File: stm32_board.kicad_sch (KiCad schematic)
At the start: 13 parts, among them SW1 SW_SPDT, U1 STM32F103C8Tx

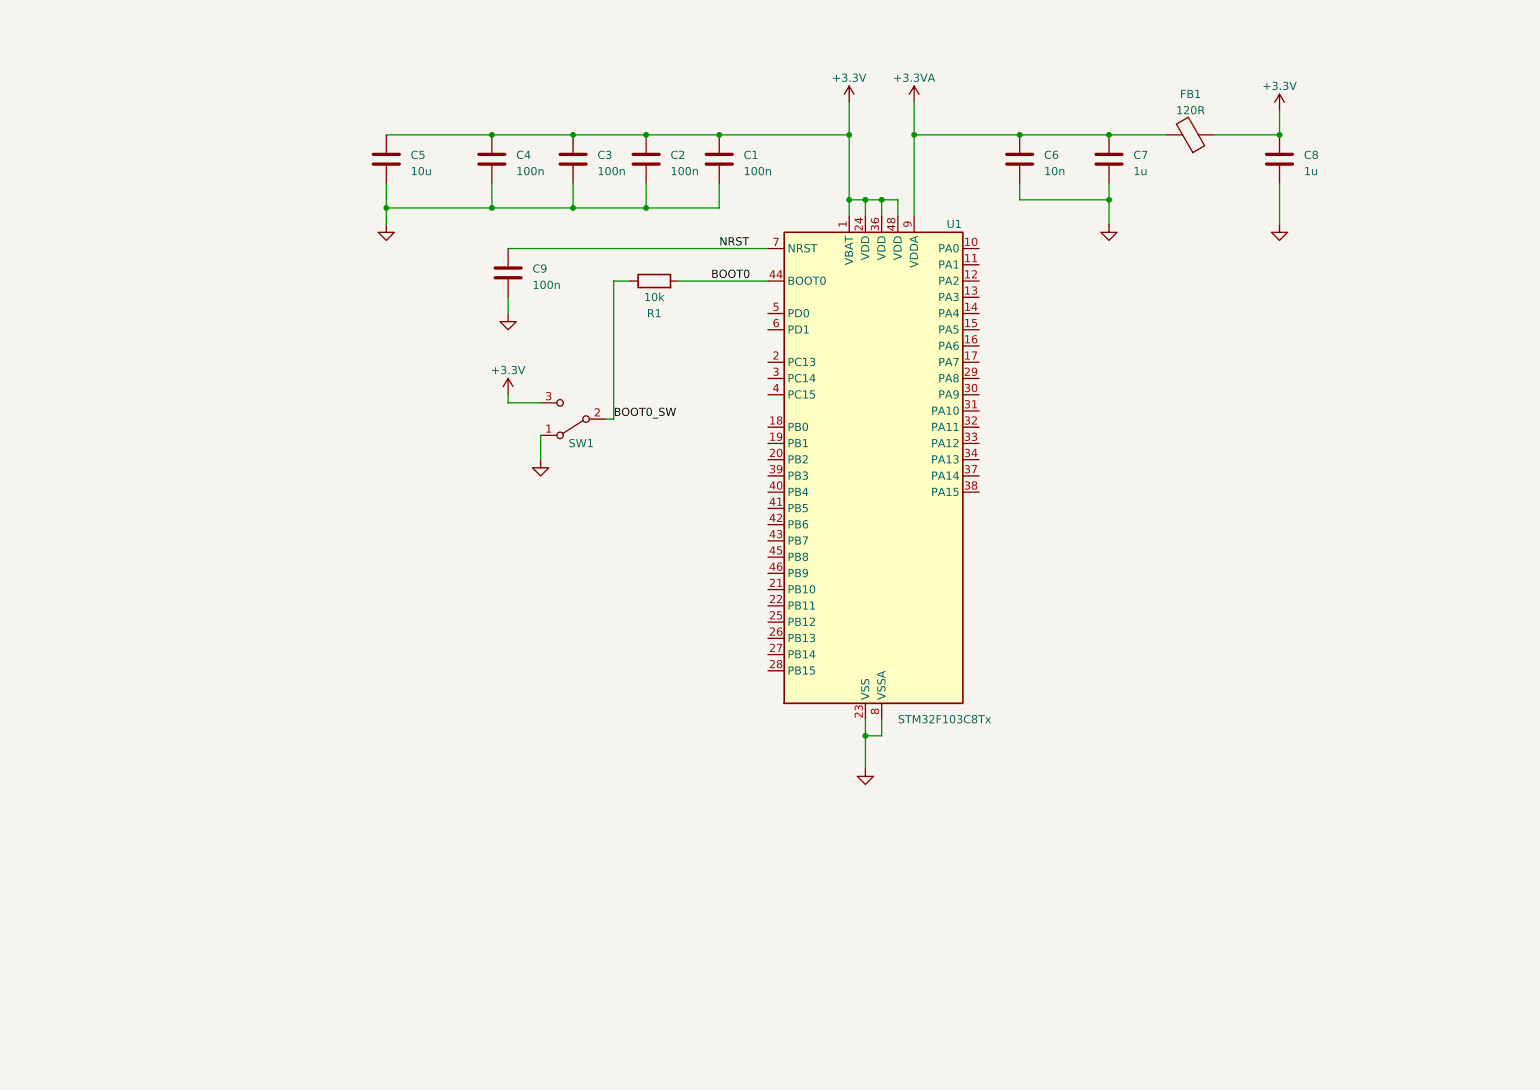
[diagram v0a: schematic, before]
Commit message: Added Crystal Oscillator
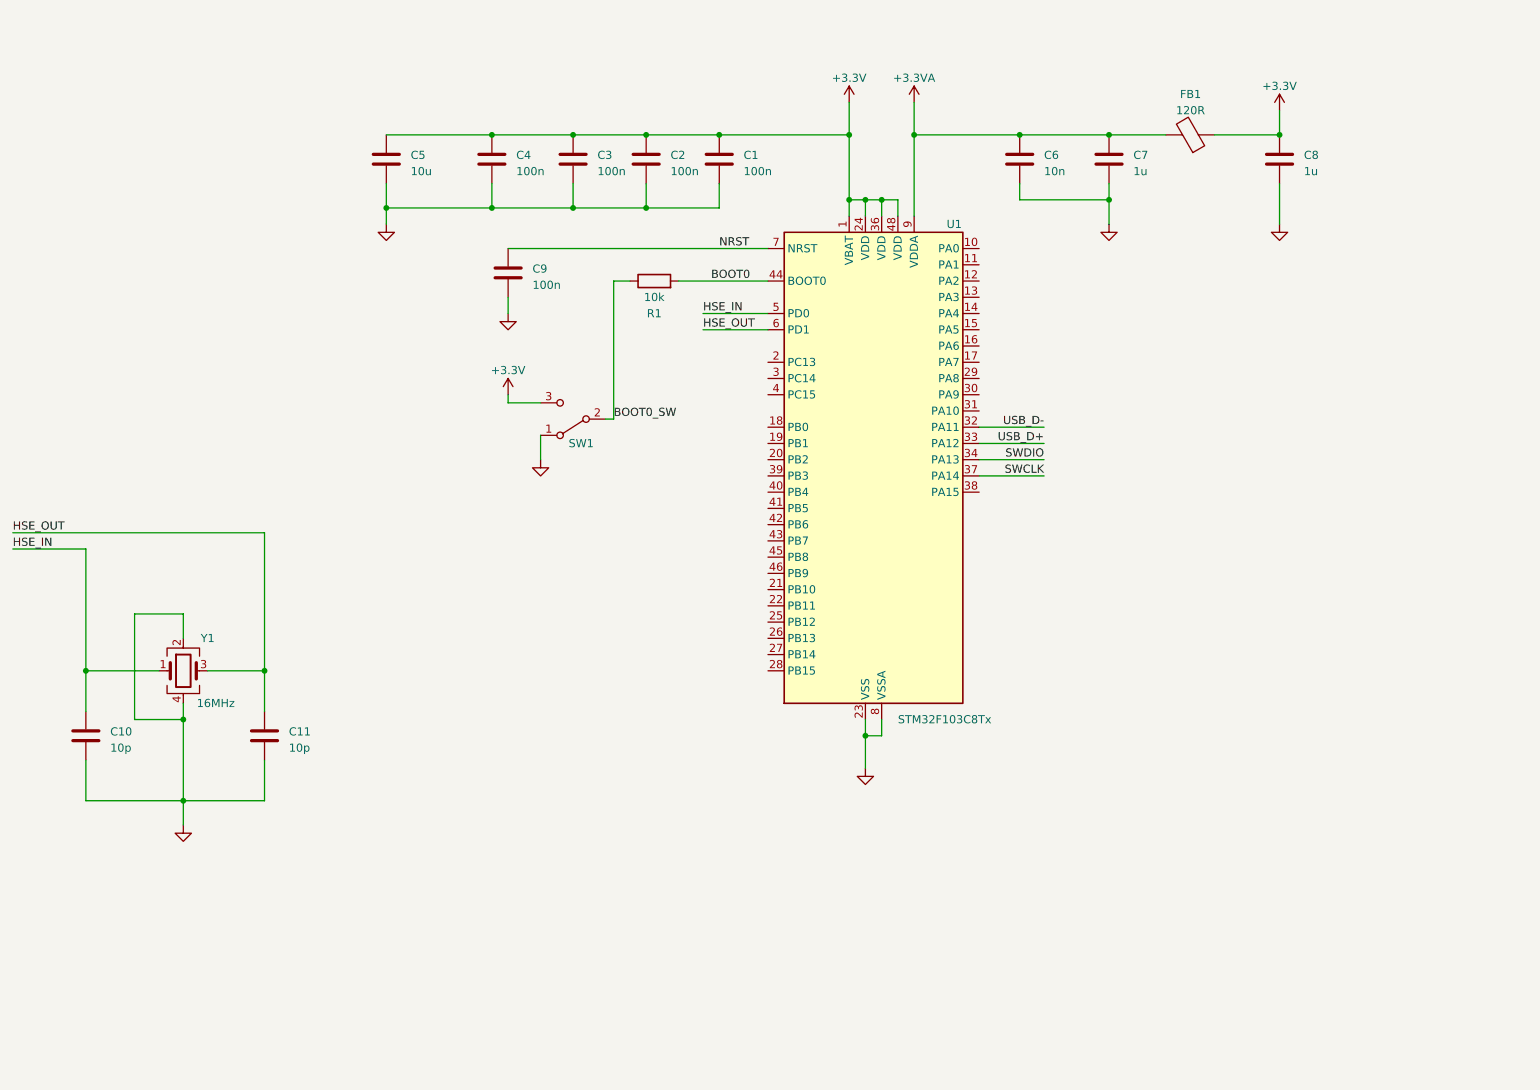
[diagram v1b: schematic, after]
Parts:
- added C10, C11: 10p, symbol Device:C
- added Y1: 16MHz, symbol Device:Crystal_GND24
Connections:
- net GND: now also C10.2, C11.2, Y1.2, Y1.4
- net USB_D-: now reaches U1.32 (PA11)
- net USB_D+: now reaches U1.33 (PA12)
- net SWDIO: now reaches U1.34 (PA13)
- net SWCLK: now reaches U1.37 (PA14)
- net HSE_IN: now reaches U1.5 (PD0)
- net HSE_IN: now also C10.1, Y1.1
- net HSE_OUT: now reaches U1.6 (PD1)
- net HSE_OUT: now also C11.1, Y1.3

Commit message: Added USB jack
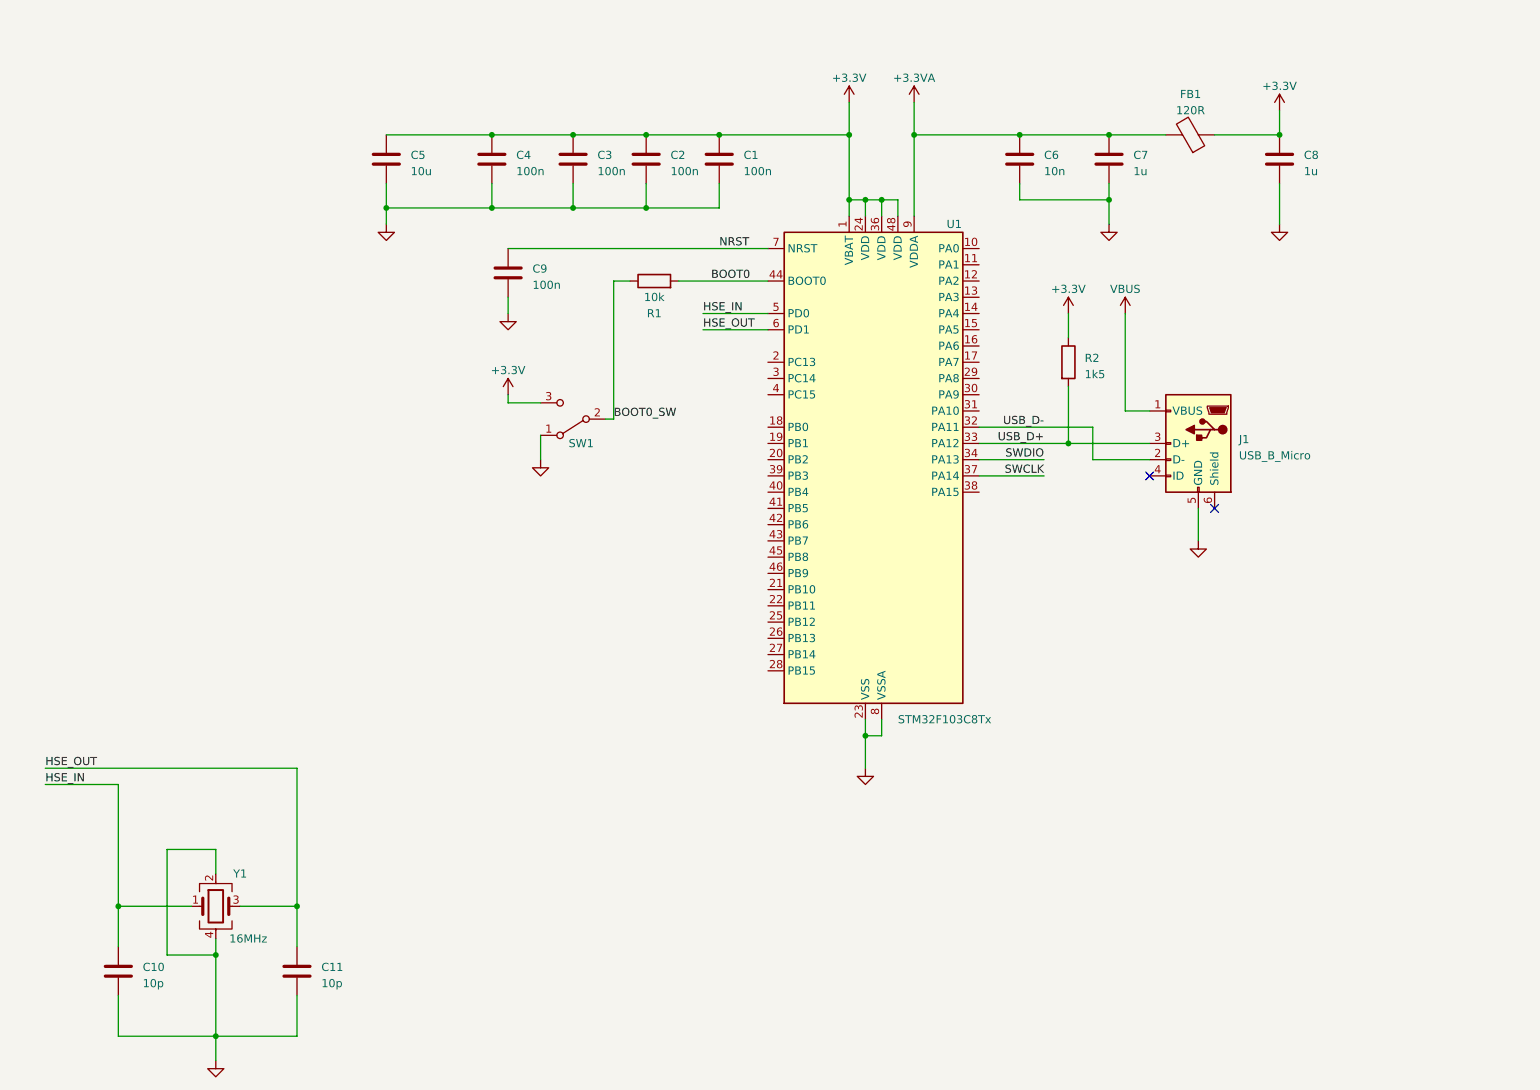
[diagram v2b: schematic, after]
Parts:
- added J1: USB_B_Micro, symbol Connector:USB_B_Micro
- added R2: 1k5, symbol Device:R
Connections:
- net +3.3V: now also R2.1
- net GND: now also J1.5 (GND)
- net USB_D+: now also J1.3 (D+), R2.2
- net USB_D-: now also J1.2 (D-)
- new net VBUS: J1.1 (VBUS)
- no-connect marks 0 -> 2
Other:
- moved on the sheet: C10, C11, Y1

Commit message: Added connectors
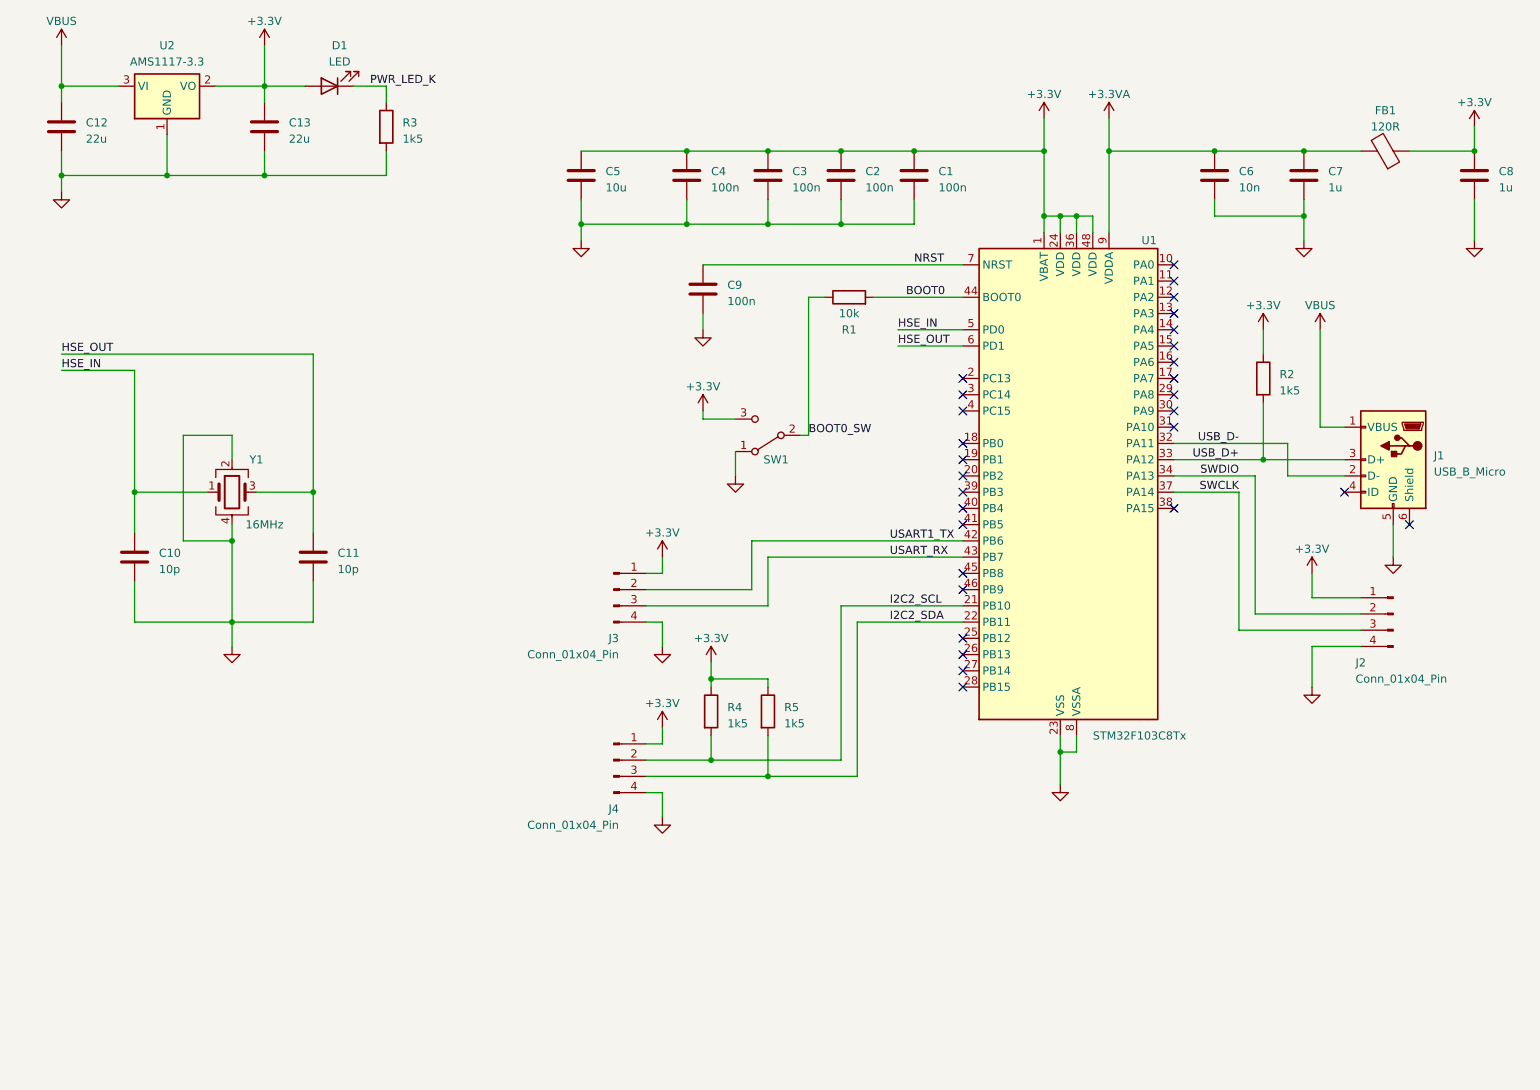
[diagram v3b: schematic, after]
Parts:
- added C12, C13: 22u, symbol Device:C
- added D1: LED, symbol Device:LED
- added J2, J3, J4: Conn_01x04_Pin, symbol Connector:Conn_01x04_Pin
- added R3, R4, R5: 1k5, symbol Device:R
- added U2: AMS1117-3.3, Package_TO_SOT_SMD:SOT-223-3_TabPin2, symbol Regulator_Linear:AMS1117-3.3
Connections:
- net +3.3V: now also C13.1, D1.2 (A), J2.1 (Pin_1), J3.1 (Pin_1), J4.1 (Pin_1), R4.1, R5.1, U2.2 (VO)
- net GND: now also C12.2, C13.2, J2.4 (Pin_4), J3.4 (Pin_4), J4.4 (Pin_4), R3.2, U2.1 (GND)
- net SWCLK: now also J2.3 (Pin_3)
- net SWDIO: now also J2.2 (Pin_2)
- net VBUS: now also C12.1, U2.3 (VI)
- net I2C2_SCL: now reaches U1.21 (PB10)
- net I2C2_SCL: now also J4.2 (Pin_2), R4.2
- net I2C2_SDA: now reaches U1.22 (PB11)
- net I2C2_SDA: now also J4.3 (Pin_3), R5.2
- net USART1_TX: now reaches U1.42 (PB6)
- net USART1_TX: now also J3.2 (Pin_2)
- net USART_RX: now reaches U1.43 (PB7)
- net USART_RX: now also J3.3 (Pin_3)
- new net PWR_LED_K: D1.1 (K), R3.1
- no-connect marks 2 -> 29
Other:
- title: (none) -> STM32 Development Board
- moved on the sheet: C1, C10, C11, C2, C3, C4, C5, C6, C7, C8, C9, FB1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

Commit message: Added notes + fixed annotations
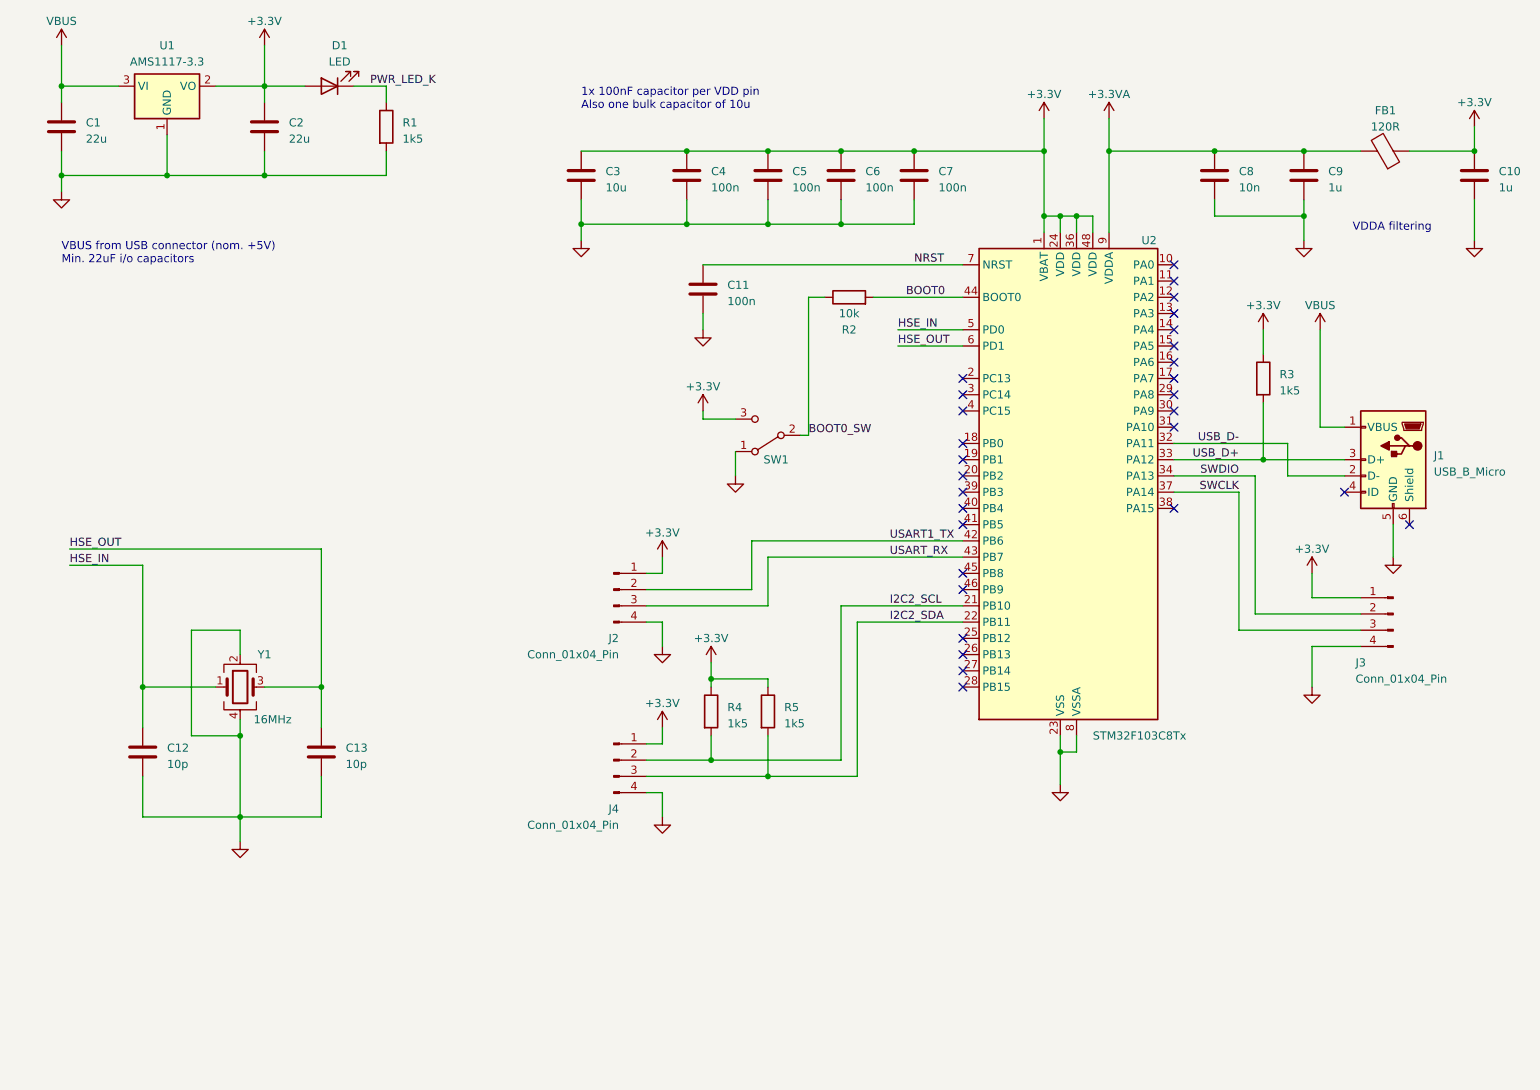
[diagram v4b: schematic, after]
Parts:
- renumbered C12 to C1, C8 to C10, C9 to C11, C10 to C12, C11 to C13, C13 to C2, C5 to C3, C3 to C5, C2 to C6, C1 to C7, C6 to C8, C7 to C9, J3 to J2, J2 to J3, R3 to R1, R1 to R2, R2 to R3, U2 to U1, U1 to U2
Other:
- note added: "1x 100nF capacitor per VDD pin Also one bulk capacitor of 10u"
- note added: "VBUS from USB connector (nom. +5V) Min. 22uF i/o capacitors"
- note added: "VDDA filtering"
- company: (none) -> devnithw
- moved on the sheet: C12, C13, Y1
